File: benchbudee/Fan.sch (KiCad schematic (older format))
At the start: 9 parts, among them Q2 MOSFET_N, Q3 MOSFET_N, Q4 MOSFET_N, U10 LM324, U11 MCP4922-E/P

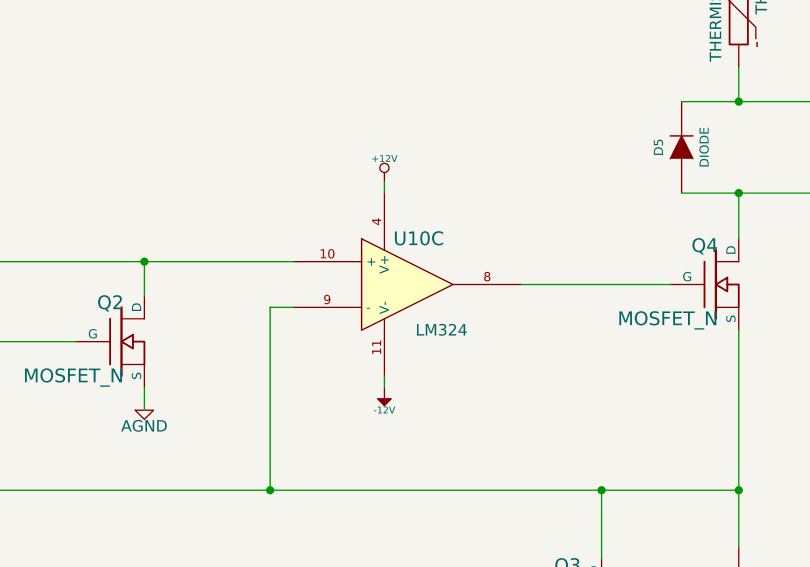
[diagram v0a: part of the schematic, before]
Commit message: Schematic and associations for the thermocouple module
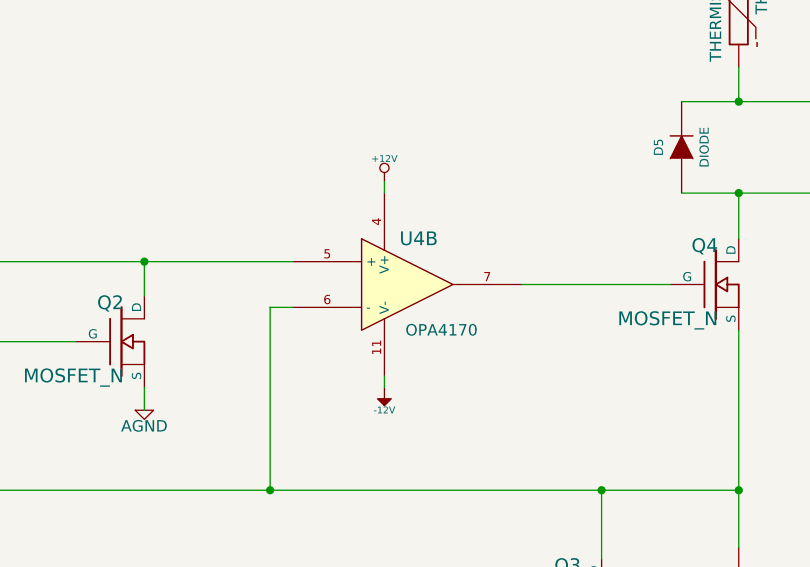
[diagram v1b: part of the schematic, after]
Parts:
- U4: renamed from U10; value LM324 -> OPA4170
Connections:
- net CURR_MEAS: now also U4.6 (-); no longer U4.9 (-)
- net at Q2.D, R25.2: now also U4.5 (+); no longer U4.10 (+)
- net at Q4.G: now also U4.7; no longer U4.8
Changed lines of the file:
@@
 FAN_PWM
 $Comp
-L LM324 U10
-U 3 1 52FBCCEC
+L LM324 U4
+U 2 1 52FBCCEC
 P 7300 2850
-F 0 "U10" H 7350 3050 60  0000 C CNN
-F 1 "LM324" H 7450 2650 50  0000 C CNN
+F 0 "U4" H 7350 3050 60  0000 C CNN
+F 1 "OPA4170" H 7450 2650 50  0000 C CNN
 F 2 "" H 7300 2850 60  0000 C CNN
 F 3 "" H 7300 2850 60  0000 C CNN
-	3    7300 2850
+	2    7300 2850
 	1    0    0    -1
 $EndComp
@@
 $EndComp
 $Comp
-L +12V #PWR048
+L +12V #PWR056
 U 1 1 52FBCDAD
 P 7200 2400
-F 0 "#PWR048" H 7200 2350 20  0001 C CNN
+F 0 "#PWR056" H 7200 2350 20  0001 C CNN
 F 1 "+12V" H 7200 2500 30  0000 C CNN
 F 2 "" H 7200 2400 60  0000 C CNN
@@
 $EndComp
 $Comp
-L -12V #PWR049
+L -12V #PWR057
 U 1 1 52FBCDD4
 P 7200 3300
-F 0 "#PWR049" H 7200 3430 20  0001 C CNN
+F 0 "#PWR057" H 7200 3430 20  0001 C CNN
 F 1 "-12V" H 7200 3400 30  0000 C CNN
 F 2 "" H 7200 3300 60  0000 C CNN
@@
 $EndComp
 $Comp
-L AGND #PWR050
+L AGND #PWR058
 U 1 1 532608FA
 P 8750 4650
-F 0 "#PWR050" H 8750 4650 40  0001 C CNN
+F 0 "#PWR058" H 8750 4650 40  0001 C CNN
 F 1 "AGND" H 8750 4580 50  0000 C CNN
 F 2 "" H 8750 4650 60  0000 C CNN
@@
 	5400 3100 5850 3100
 $Comp
-L AGND #PWR051
+L AGND #PWR059
 U 1 1 53260B07
 P 6150 3400
-F 0 "#PWR051" H 6150 3400 40  0001 C CNN
+F 0 "#PWR059" H 6150 3400 40  0001 C CNN
 F 1 "AGND" H 6150 3330 50  0000 C CNN
 F 2 "" H 6150 3400 60  0000 C CNN
@@
 FAN_MODE
 $Comp
-L +12C #PWR052
+L +12C #PWR060
 U 1 1 53261310
 P 8750 1300
-F 0 "#PWR052" H 8750 1270 30  0001 C CNN
+F 0 "#PWR060" H 8750 1270 30  0001 C CNN
 F 1 "+12C" H 8750 1410 40  0000 C CNN
 F 2 "" H 8750 1300 60  0000 C CNN

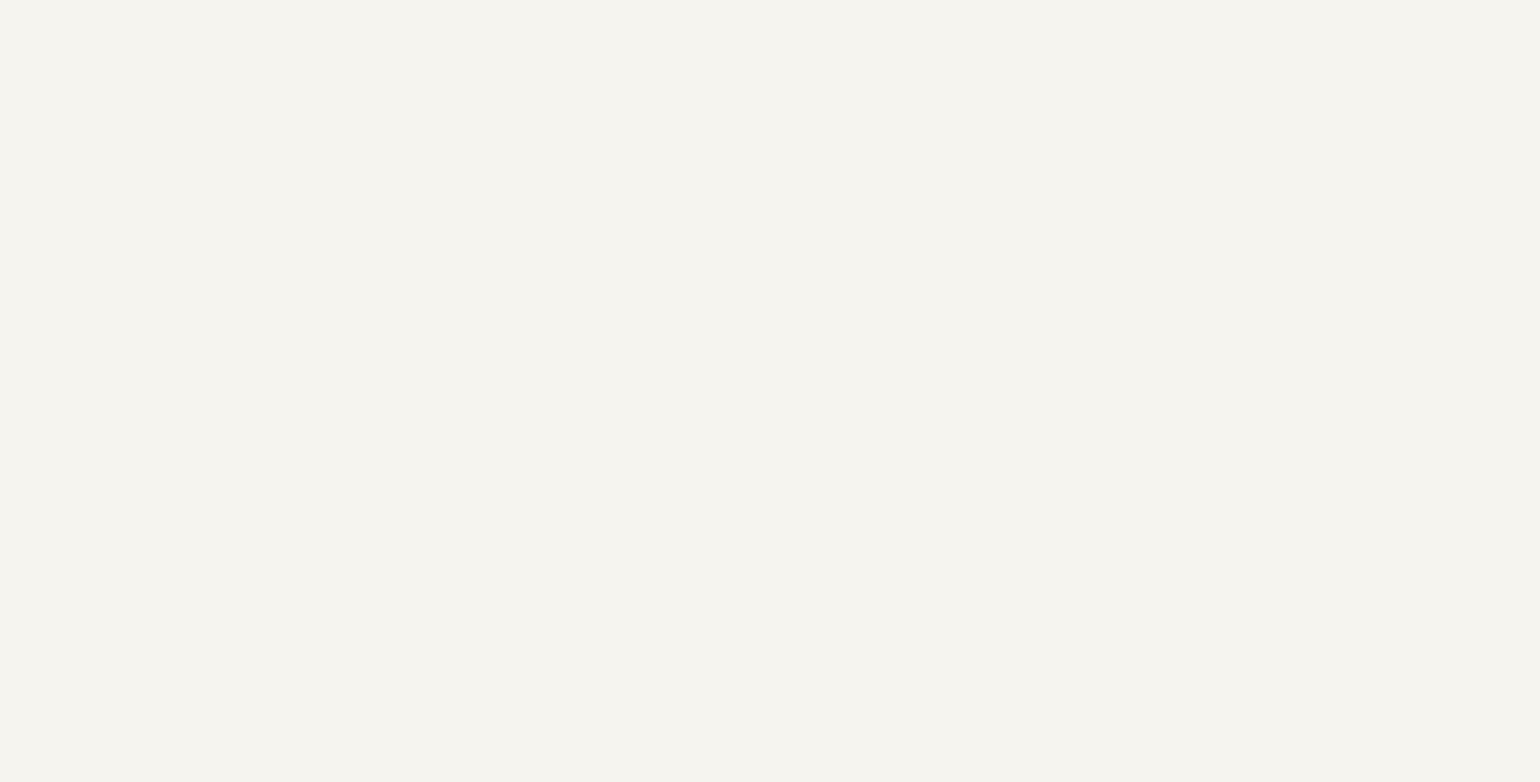
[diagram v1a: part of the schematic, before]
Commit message: Initial placement of thermocouple module
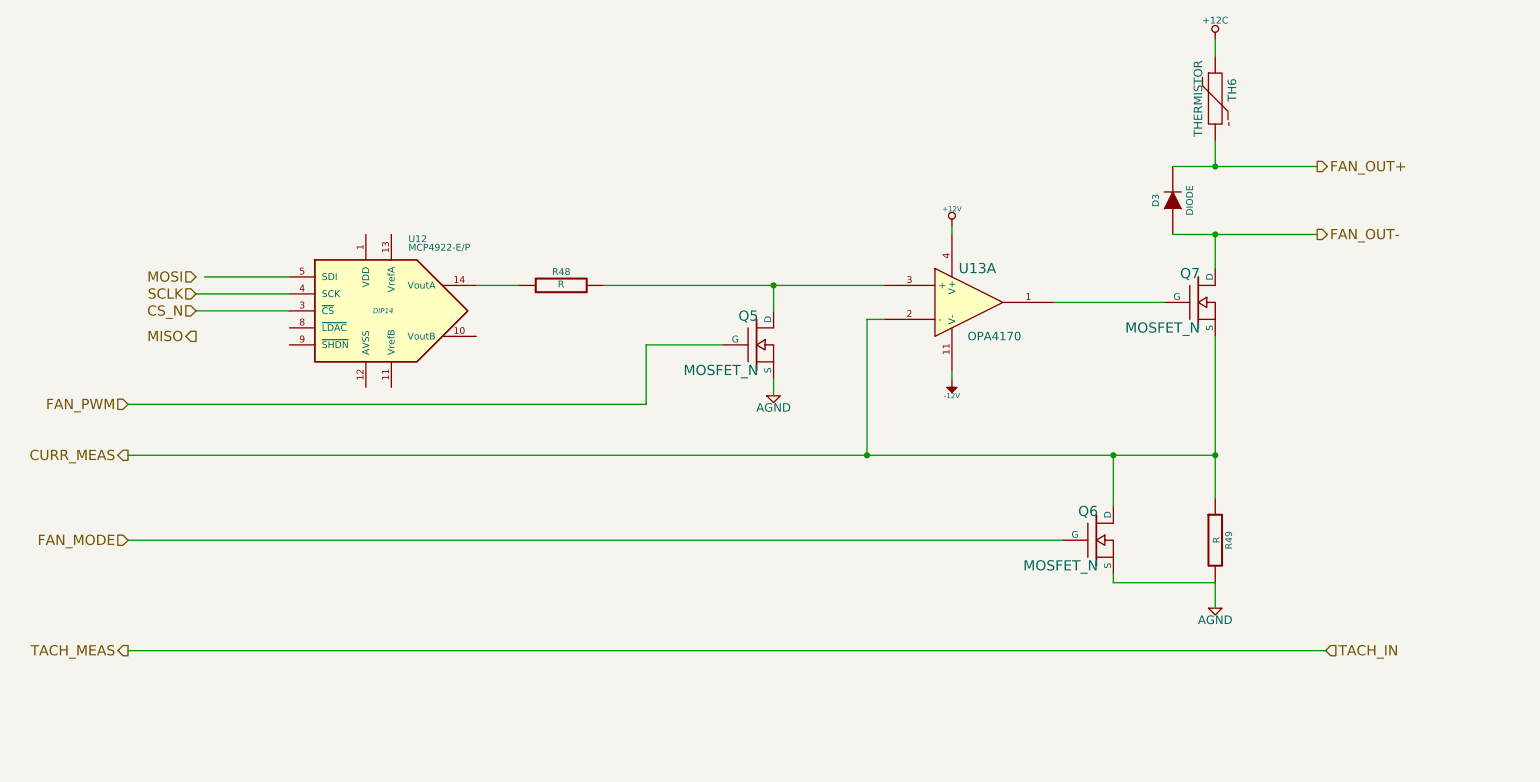
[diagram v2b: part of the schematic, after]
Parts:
- added D3: DIODE, symbol DIODE
- added Q5, Q6, Q7: MOSFET_N, ~, symbol MOSFET_N
- added R48: R, ~, symbol R
- added R49: R, symbol R
- added TH6: THERMISTOR, symbol THERMISTOR
- added U12: MCP4922-E/P, DIP14, symbol MCP4922-E/P
- added U13: OPA4170, symbol LM324
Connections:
- net +12C: now also TH6.1
- net +12V: now also U13.4 (V+)
- net -12V: now also U13.11 (V-)
- net AGND: now also Q5.S, Q6.S, R49.2
- net CS_N: now also U12.3 (~CS~)
- net CURR_MEAS: now also Q6.D, Q7.S, R49.1, U13.2 (-)
- net FAN_MODE: now also Q6.G
- net FAN_OUT+: now also D3.2 (K), TH6.2
- net FAN_OUT-: now also D3.1 (A), Q7.D
- net FAN_PWM: now also Q5.G
- net SCLK: now also U12.4 (SCK)
- new net: Q7.G, U13.1
- new net: Q5.D, R48.2, U13.3 (+)
- new net: R48.1, U12.14 (VoutA)
